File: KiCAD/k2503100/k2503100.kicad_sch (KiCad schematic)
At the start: 4 parts, among them SW1 SW_Push, SW2 SW_Push, SW3 SW_Push, U101 Teensy4.1

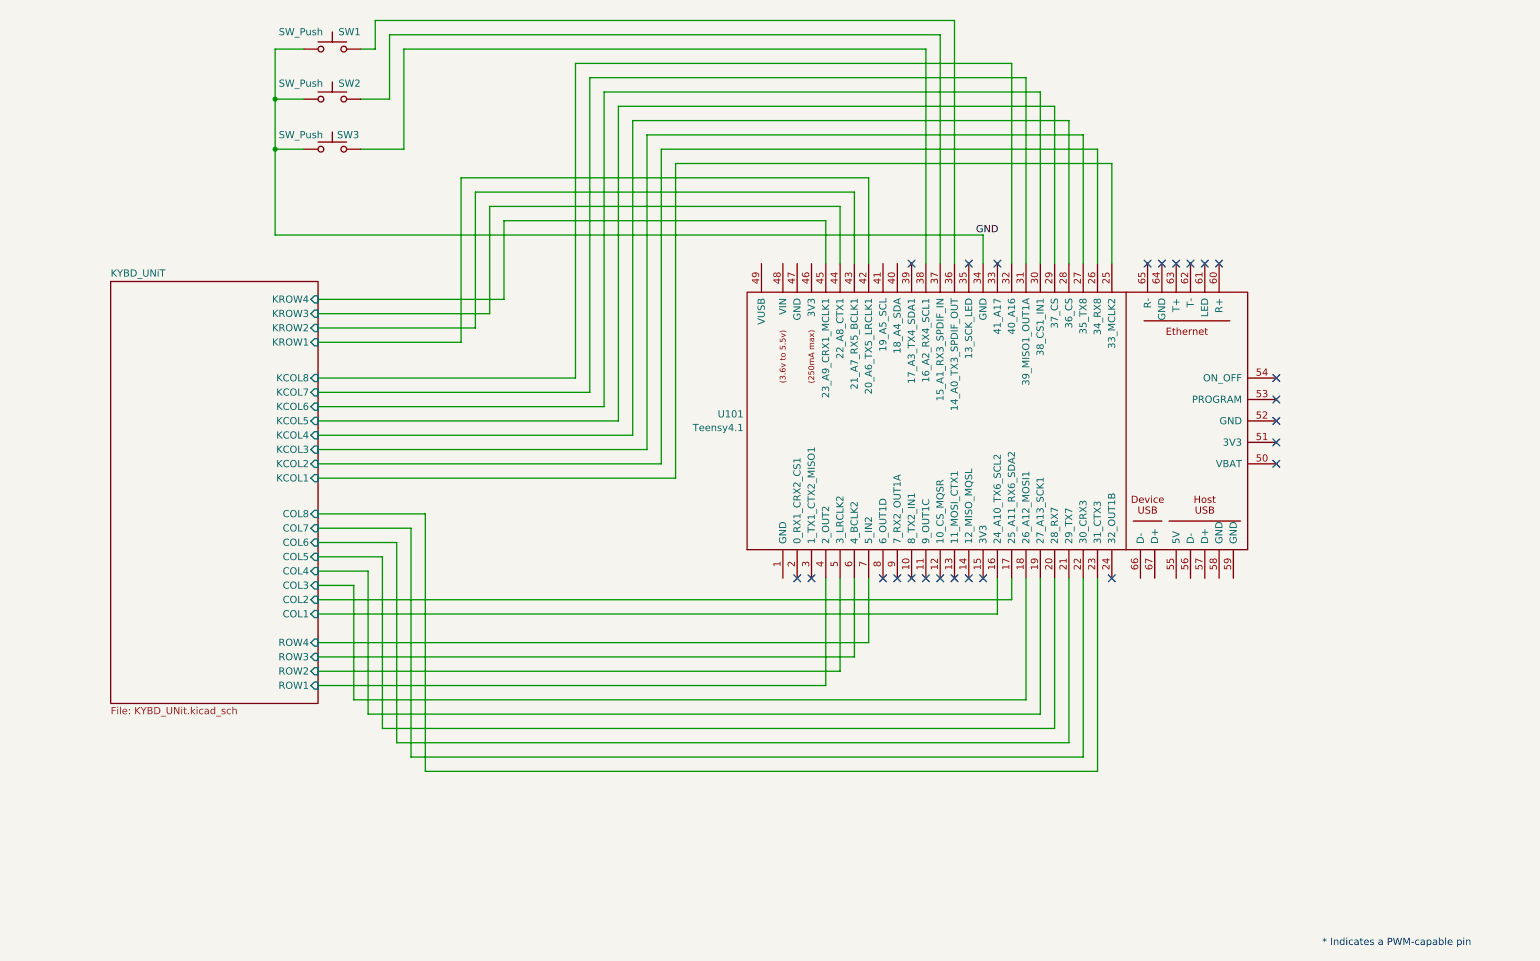
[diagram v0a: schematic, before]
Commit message: LCDとVRコネクタ追加
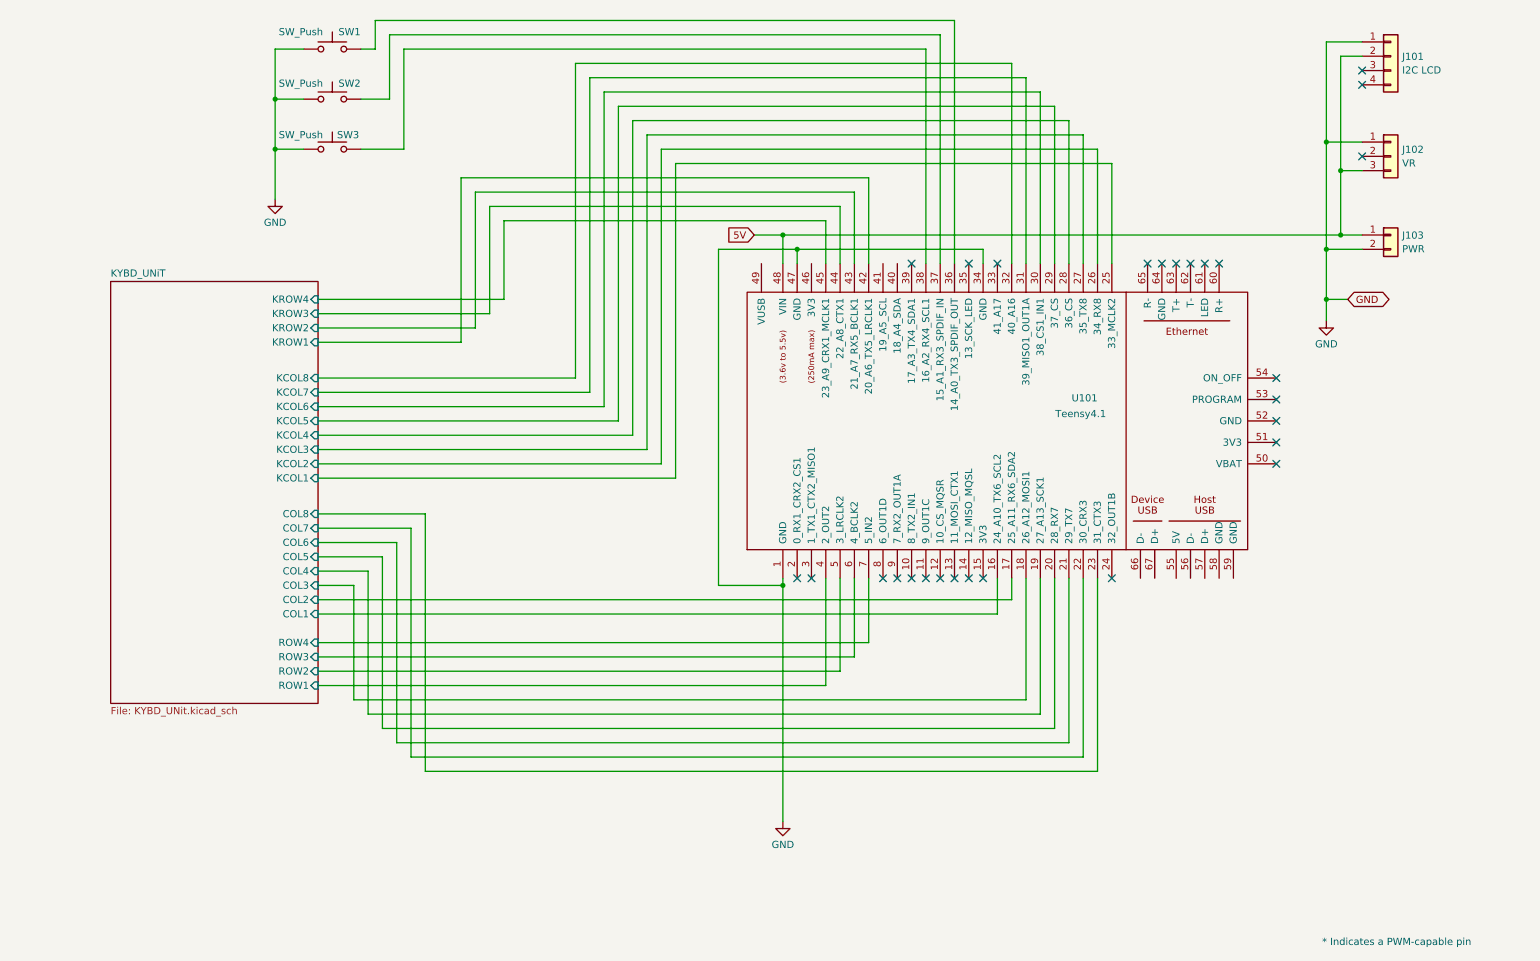
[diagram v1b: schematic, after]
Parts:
- added J101: I2C LCD, Connector_JST:JST_XH_S4B-XH-A_1x04_P2.50mm_Horizontal, symbol Connector_Generic:Conn_01x04
- added J102: VR, Connector_JST:JST_XH_S3B-XH-A_1x03_P2.50mm_Horizontal, symbol Connector_Generic:Conn_01x03
- added J103: PWR, Connector_JST:JST_XH_S2B-XH-A_1x02_P2.50mm_Horizontal, symbol Connector_Generic:Conn_01x02
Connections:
- net GND: now also U101.1 (GND), U101.47 (GND), J101.1 (Pin_1), J102.1 (Pin_1), J103.2 (Pin_2)
- net 5V: now reaches U101.48 (VIN)
- net 5V: now also J101.2 (Pin_2), J102.3 (Pin_3), J103.1 (Pin_1)
- no-connect marks 25 -> 28

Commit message: 寸法図途中
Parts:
- added U1: AE-PCA9306, Package_DIP:DIP-8_W7.62mm, symbol HOLLY2:AE-PCA9306
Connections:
- net 5V: now also U1.8 (VREF2); no longer J102.3 (Pin_3)
- net GND: now also U1.5 (GND)
- net at J102.2 (Pin_2): now also U101.33 (41_A17)
- net at U101.40 (18_A4_SDA): now also U1.3 (SDA1)
- net at U101.41 (19_A5_SCL): now also U1.2 (SCL1)
- net +3.3V: now reaches U101.46 (3V3)
- net +3.3V: now also J102.3 (Pin_3), U1.1 (VREF1)
- net SDA_H: now reaches J101.3 (Pin_3)
- net SDA_H: now also U1.6 (SDA2)
- net SCL_H: now reaches J101.4 (Pin_4)
- net SCL_H: now also U1.7 (SCL2)
- no-connect marks 28 -> 25
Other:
- moved on the sheet: J101, J102, J103

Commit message: PCB発注とソフト開発
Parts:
- added Q1, Q2, Q3: NNBT3904, Package_TO_SOT_SMD:SOT-23_Handsoldering, symbol Transistor_BJT:2N3904
- added R1, R4, R6: 4.7k, Resistor_SMD:R_0603_1608Metric_Pad0.98x0.95mm_HandSolder, symbol Device:R_US
- added R2, R3, R5: 100, Resistor_SMD:R_0603_1608Metric_Pad0.98x0.95mm_HandSolder, symbol Device:R_US
- added TP1, TP2: TestPoint, TestPoint:TestPoint_Pad_D2.0mm, symbol Connector:TestPoint
- SW1: value SW_Push -> サイレンテスト; symbol Switch:SW_Push -> K2503100:MP86A1
- SW2: value SW_Push -> 緊急停止; symbol Switch:SW_Push -> K2503100:MP86A1
- SW3: value SW_Push -> 放送開始; symbol Switch:SW_Push -> K2503100:MP86A1
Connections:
- net 5V: now also Q1.3 (C), Q2.3 (C), Q3.3 (C)
- net GND: now also R2.2, R3.2, R5.2
- net at U101.10 (8_TX2_IN1): now also R1.2
- new net: Q2.1 (E), SW2.4
- new net: R3.1, SW2.5
- new net: Q2.2 (B), R4.1
- new net: R4.2, TP2.1
- new net: R6.2, TP1.1
- new net: Q3.1 (E), SW1.4
- new net: R5.1, SW1.5
- new net: Q1.1 (E), SW3.4
- new net: R2.1, SW3.5
- new net: Q3.2 (B), R6.1
- new net: Q1.2 (B), R1.1
- no-connect marks 25 -> 30

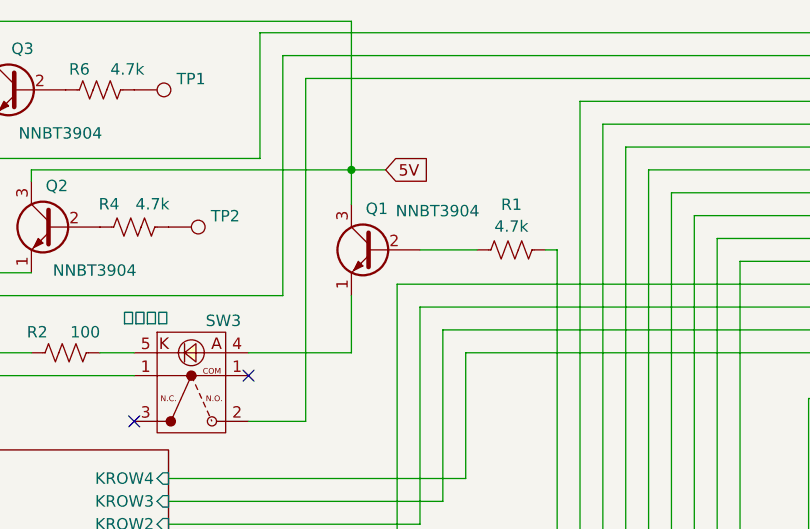
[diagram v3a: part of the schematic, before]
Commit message: MMBT3904に変更を開始
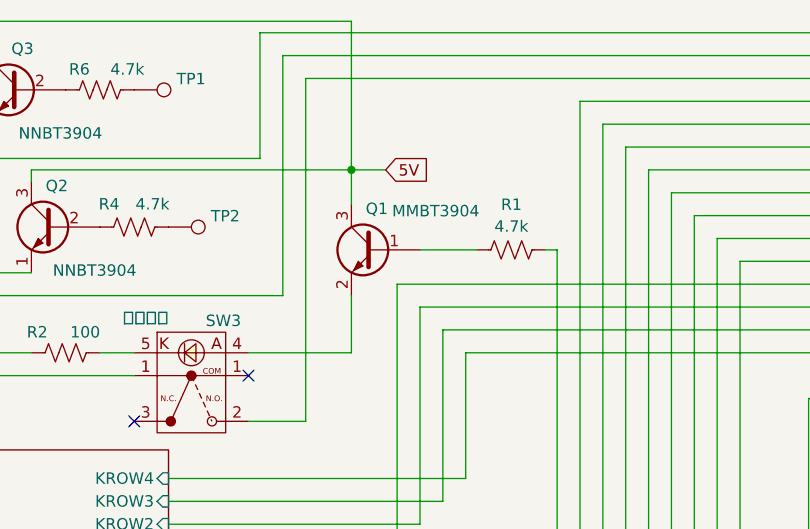
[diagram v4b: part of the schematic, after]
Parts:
- Q1: value NNBT3904 -> MMBT3904; footprint Package_TO_SOT_SMD:SOT-23_Handsoldering -> Package_TO_SOT_SMD:SOT-23; symbol Transistor_BJT:2N3904 -> Transistor_BJT:MMBT3904
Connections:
- net at SW3.4: now also Q1.2 (E); no longer Q1.1 (E)
- net at R1.1: now also Q1.1 (B); no longer Q1.2 (B)
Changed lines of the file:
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@@
 	)
 	(symbol
-		(lib_id "Transistor_BJT:2N3904")
+		(lib_id "Transistor_BJT:MMBT3904")
 		(at 96.52 39.37 0)
 		(mirror y)
@@
 			)
 		)
-		(property "Value" "NNBT3904"
+		(property "Value" "MMBT3904"
 			(at 108.204 35.052 0)
 			(effects
@@
 			)
 		)
-		(property "Footprint" "Package_TO_SOT_SMD:SOT-23_Handsoldering"
+		(property "Footprint" "Package_TO_SOT_SMD:SOT-23"
 			(at 91.44 41.275 0)
 			(effects
@@
 			)
 		)
-		(property "Datasheet" "https://akizukidenshi.com/goodsaffix/2N3904_MMBT3904_PZT3904.pdf"
+		(property "Datasheet" "https://www.onsemi.com/pdf/datasheet/pzt3904-d.pdf"
 			(at 96.52 39.37 0)
 			(effects
@@
 			)
 		)
-		(property "Description" "0.2A Ic, 40V Vce, Small Signal NPN Transistor, TO-92"
+		(property "Description" "0.2A Ic, 40V Vce, Small Signal NPN Transistor, SOT-23"
 			(at 96.52 39.37 0)
 			(effects

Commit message: MMBT3904変更済み
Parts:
- Q2, Q3: value NNBT3904 -> MMBT3904; footprint Package_TO_SOT_SMD:SOT-23_Handsoldering -> Package_TO_SOT_SMD:SOT-23; symbol Transistor_BJT:2N3904 -> Transistor_BJT:MMBT3904
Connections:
- net at SW2.4: now also Q2.2 (E); no longer Q2.1 (E)
- net at R4.1: now also Q2.1 (B); no longer Q2.2 (B)
- net at SW1.4: now also Q3.2 (E); no longer Q3.1 (E)
- net at R6.1: now also Q3.1 (B); no longer Q3.2 (B)
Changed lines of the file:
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@@
 	(title_block
 		(title "k2503100 操作パネル")
-		(date "2025-02-04")
-		(rev "1.10")
+		(date "2025-03-25")
+		(rev "2.00")
 		(company "HOLLY&Co.,Ltd. Masafumi Horimoto")
+		(comment 1 "MMBT3904シンボル変更")
 	)
 	(junction
@@
 	)
 	(symbol
-		(lib_id "Transistor_BJT:2N3904")
+		(lib_id "Transistor_BJT:MMBT3904")
 		(at 60.96 36.83 0)
 		(mirror y)
@@
 			)
 		)
-		(property "Value" "NNBT3904"
+		(property "Value" "MMBT3904"
 			(at 70.104 41.656 0)
 			(effects
@@
 			)
 		)
-		(property "Footprint" "Package_TO_SOT_SMD:SOT-23_Handsoldering"
+		(property "Footprint" "Package_TO_SOT_SMD:SOT-23"
 			(at 55.88 38.735 0)
 			(effects
@@
 			)
 		)
-		(property "Datasheet" "https://akizukidenshi.com/goodsaffix/2N3904_MMBT3904_PZT3904.pdf"
+		(property "Datasheet" "https://www.onsemi.com/pdf/datasheet/pzt3904-d.pdf"
 			(at 60.96 36.83 0)
 			(effects
@@
 			)
 		)
-		(property "Description" "0.2A Ic, 40V Vce, Small Signal NPN Transistor, TO-92"
+		(property "Description" "0.2A Ic, 40V Vce, Small Signal NPN Transistor, SOT-23"
 			(at 60.96 36.83 0)
 			(effects
@@
 	)
 	(symbol
-		(lib_id "Transistor_BJT:2N3904")
+		(lib_id "Transistor_BJT:MMBT3904")
 		(at 57.15 21.59 0)
 		(mirror y)
@@
 			)
 		)
-		(property "Value" "NNBT3904"
+		(property "Value" "MMBT3904"
 			(at 66.294 26.416 0)
 			(effects
@@
 			)
 		)
-		(property "Footprint" "Package_TO_SOT_SMD:SOT-23_Handsoldering"
+		(property "Footprint" "Package_TO_SOT_SMD:SOT-23"
 			(at 52.07 23.495 0)
 			(effects
@@
 			)
 		)
-		(property "Datasheet" "https://akizukidenshi.com/goodsaffix/2N3904_MMBT3904_PZT3904.pdf"
+		(property "Datasheet" "https://www.onsemi.com/pdf/datasheet/pzt3904-d.pdf"
 			(at 57.15 21.59 0)
 			(effects
@@
 			)
 		)
-		(property "Description" "0.2A Ic, 40V Vce, Small Signal NPN Transistor, TO-92"
+		(property "Description" "0.2A Ic, 40V Vce, Small Signal NPN Transistor, SOT-23"
 			(at 57.15 21.59 0)
 			(effects
